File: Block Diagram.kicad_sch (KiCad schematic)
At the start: 0 parts

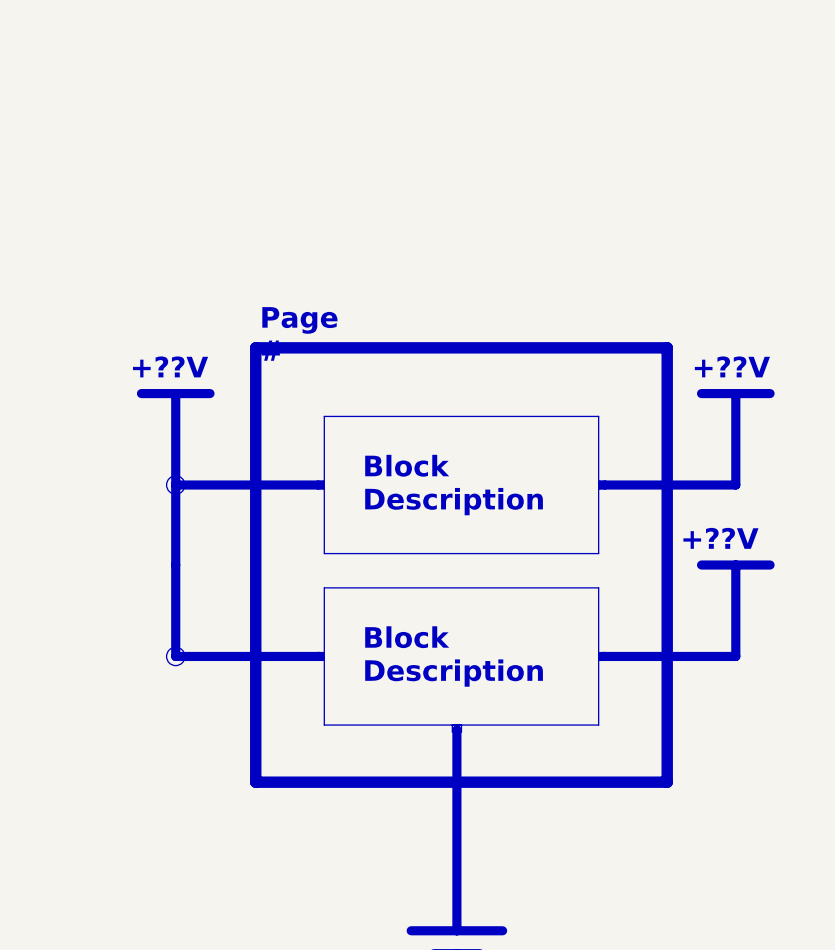
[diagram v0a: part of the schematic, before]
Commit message: Add MCU Power schematic
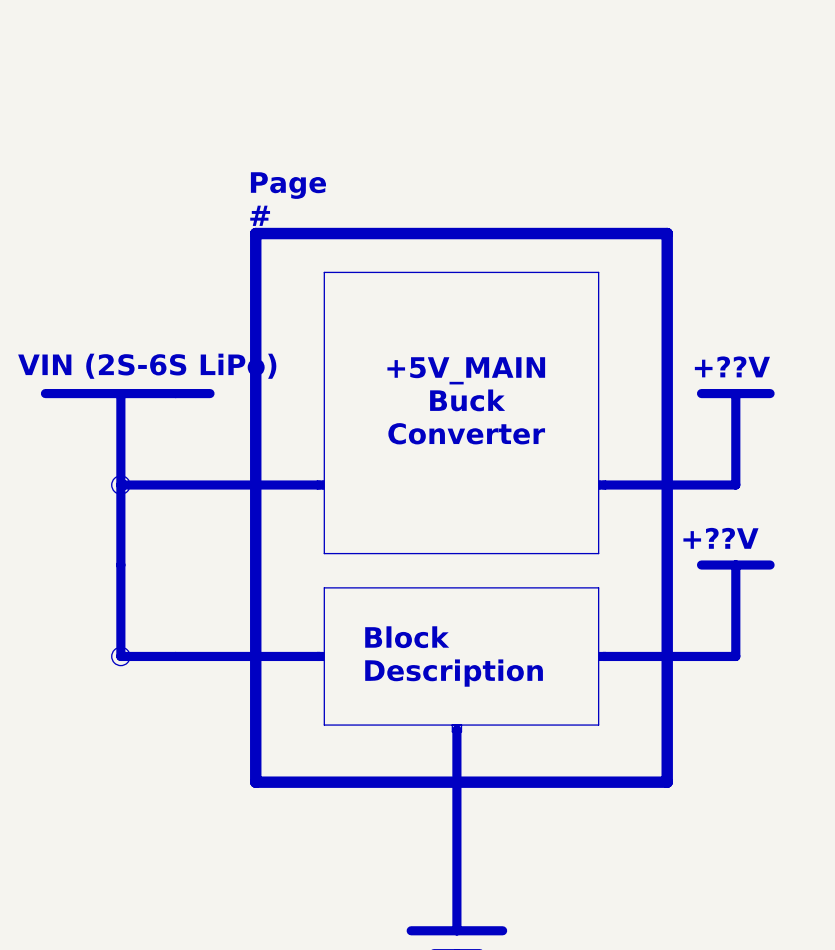
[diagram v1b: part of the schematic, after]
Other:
- note added: "VIN (2S-6S LiPo)"
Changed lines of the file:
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@@
 	)
 	(rectangle
-		(start 74.168 82.55)
+		(start 74.168 66.548)
 		(end 104.648 97.79)
 		(stroke
@@
 	)
 	(circle
-		(center 57.658 109.22)
+		(center 51.562 109.22)
 		(radius 1.016)
 		(stroke
@@
 	)
 	(rectangle
-		(start 66.548 74.93)
+		(start 66.548 62.23)
 		(end 112.268 123.19)
 		(stroke
@@
 	)
 	(circle
-		(center 57.658 90.17)
+		(center 51.562 90.17)
 		(radius 1.016)
 		(stroke
@@
 		)
 	)
-	(text "+??V"
-		(exclude_from_sim no)
-		(at 52.578 78.74 0)
+	(text "VIN (2S-6S LiPo)"
+		(exclude_from_sim no)
+		(at 40.132 78.486 0)
 		(effects
 			(font
@@
 	(text_box "Page #"
 		(exclude_from_sim no)
-		(at 65.278 68.58 0)
+		(at 64.008 53.594 0)
 		(size 13.97 5.08)
 		(margins 1.7144 1.7144 1.7144 1.7144)
@@
 		)
 	)
-	(text_box "Block\nDescription"
-		(exclude_from_sim no)
-		(at 76.708 85.09 0)
-		(size 25.4 10.16)
-		(margins 1.7144 1.7144 1.7144 1.7144)
-		(stroke
-			(width -0.0001)
-			(type default)
+	(text_box "+5V_MAIN Buck Converter"
+		(exclude_from_sim no)
+		(at 77.216 74.1471 0)
+		(size 25.4 22.8809)
+		(margins 1.7144 1.7144 1.7144 1.7144)
+		(stroke
+			(width -0.0001)
+			(type solid)
 		)
 		(fill
@@
 				(color 0 0 0 1)
 			)
-			(justify left top)
+			(justify top)
 		)
 	)
@@
 	(polyline
 		(pts
-			(xy 57.658 80.01) (xy 57.658 90.17)
+			(xy 51.562 80.01) (xy 51.562 90.17)
 		)
 		(stroke
@@
 	(polyline
 		(pts
-			(xy 57.658 99.06) (xy 57.658 109.22)
+			(xy 51.562 99.06) (xy 51.562 109.22)
 		)
 		(stroke
@@
 	(polyline
 		(pts
-			(xy 57.658 90.17) (xy 57.658 99.06)
+			(xy 51.562 90.17) (xy 51.562 99.06)
 		)
 		(stroke
@@
 	(polyline
 		(pts
-			(xy 73.66 90.17) (xy 57.658 90.17)
+			(xy 73.66 90.17) (xy 51.562 90.17)
 		)
 		(stroke
@@
 	(polyline
 		(pts
-			(xy 53.848 80.01) (xy 57.658 80.01)
+			(xy 43.18 80.01) (xy 57.658 80.01)
 		)
 		(stroke
@@
 		)
 	)
+	(polyline
+		(pts
+			(xy 51.562 109.22) (xy 57.658 109.22)
+		)
+		(stroke
+			(width 1.016)
+			(type default)
+			(color 198 71 194 1)
+		)
+	)
